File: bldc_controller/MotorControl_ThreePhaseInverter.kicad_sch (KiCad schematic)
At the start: 42 parts, among them J11 Phase A, J12 Phase B, J13 Phase C, Q1 TPH2R408QM,L1Q, Q2 TPH2R408QM,L1Q, Q3 TPH2R408QM,L1Q, Q4 TPH2R408QM,L1Q, Q5 TPH2R408QM,L1Q, Q6 TPH2R408QM,L1Q

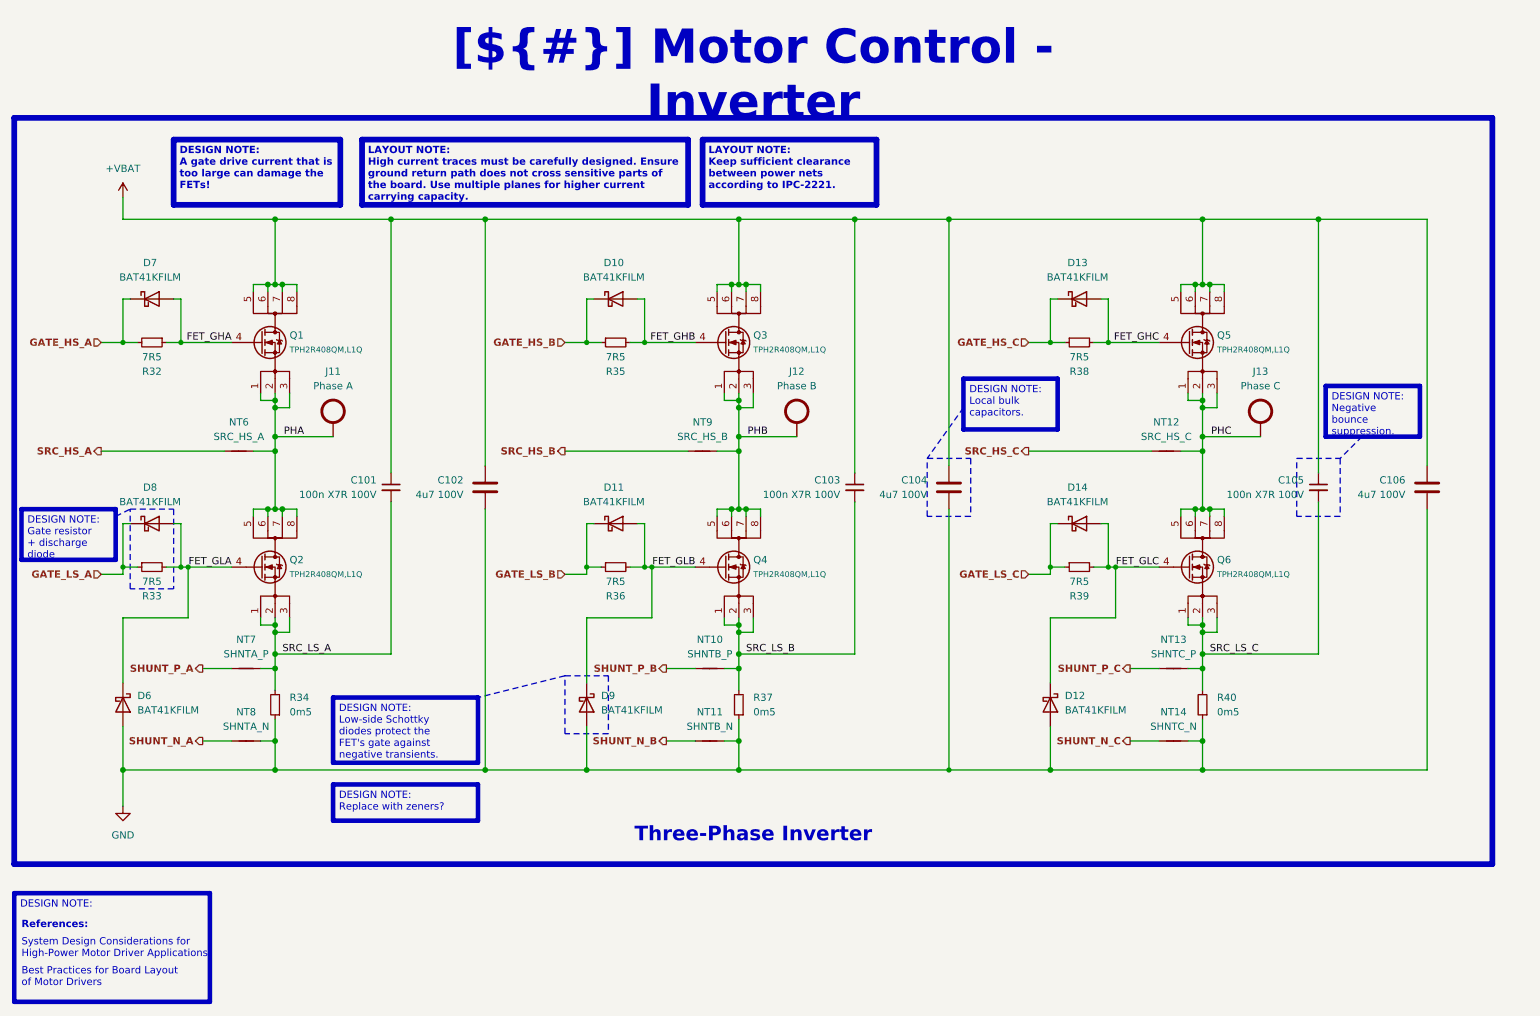
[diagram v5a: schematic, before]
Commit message: routed all signals. TODO: redo all power polygons and ensure good return paths/reference. Added 3d models
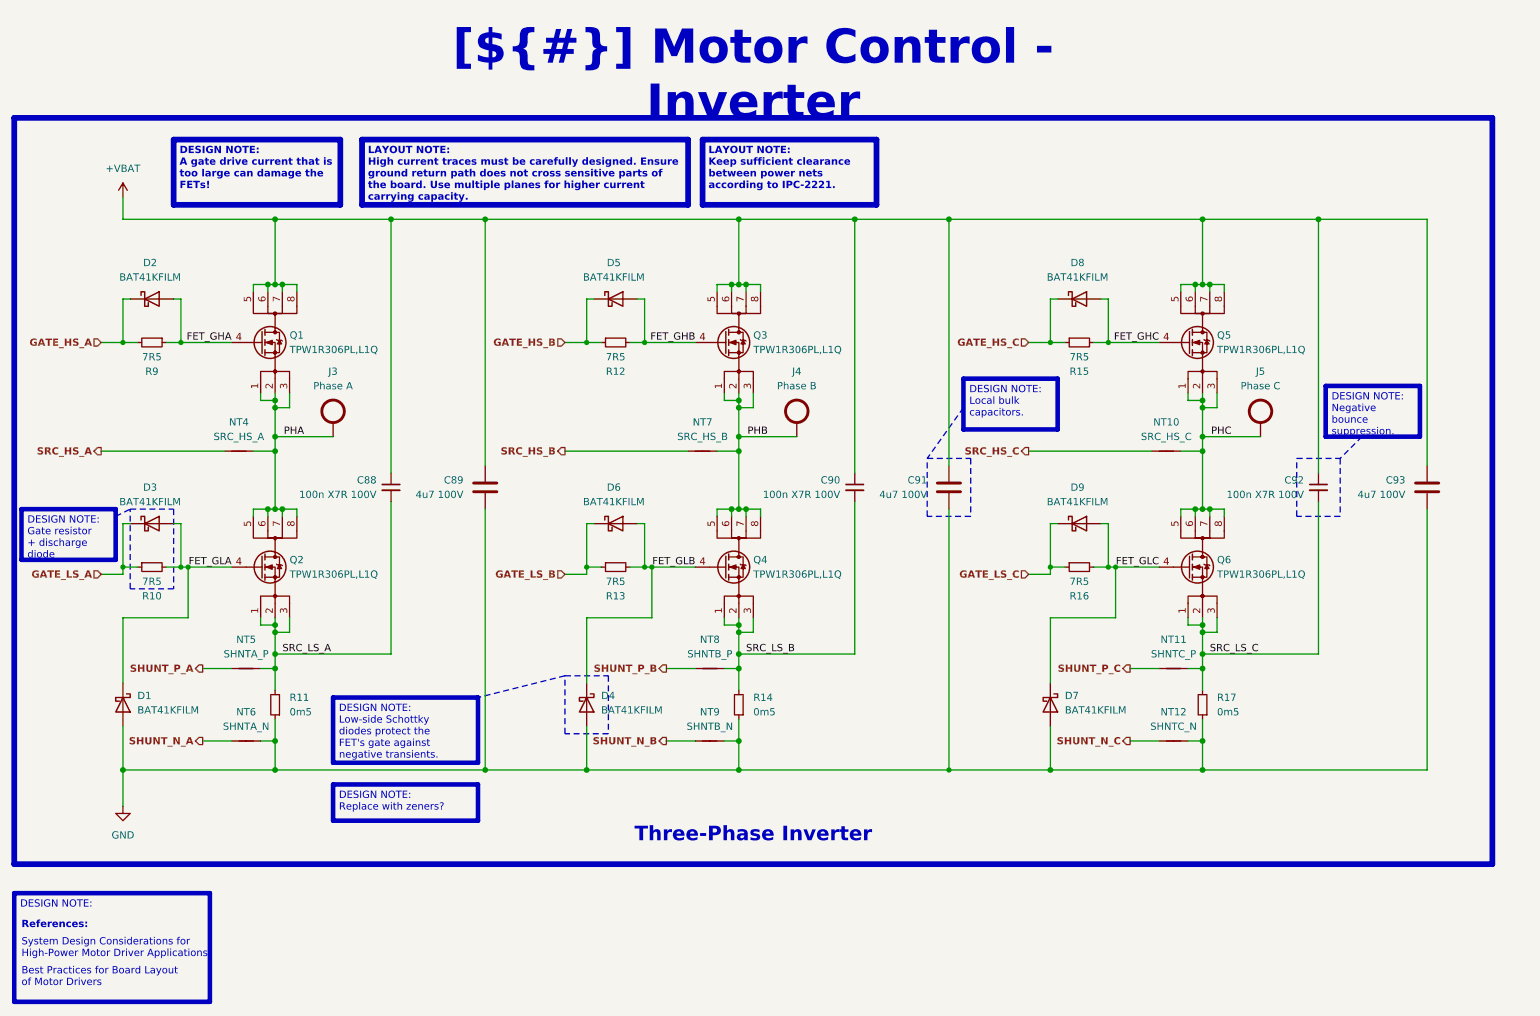
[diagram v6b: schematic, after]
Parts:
- removed Q1, Q2, Q3, Q4, Q5, Q6: TPH2R408QM,L1Q, 0_transistor_fet:2-5Q1S, symbol 0_transistor_fet:TPH2R408QM,L1Q
- added Q1, Q2, Q3, Q4, Q5, Q6: TPW1R306PL,L1Q, 0_transistor_fet:2-5S1A, symbol 0_transistor_fet:TPW1R306PL,L1Q
- renumbered C101 to C88, C102 to C89, C103 to C90, C104 to C91, C105 to C92, C106 to C93, D6 to D1, D7 to D2, D8 to D3, D9 to D4, D10 to D5, D11 to D6, D12 to D7, D13 to D8, D14 to D9, J11 to J3, J12 to J4, J13 to J5, NT12 to NT10, NT13 to NT11, NT14 to NT12, NT6 to NT4, NT7 to NT5, NT8 to NT6, NT9 to NT7, NT10 to NT8, NT11 to NT9, R33 to R10, R34 to R11, R35 to R12, R36 to R13, R37 to R14, R38 to R15, R39 to R16, R40 to R17, R32 to R9
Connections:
- net +VBAT: now also Q1.5 (D), Q1.6 (D), Q1.7 (D), Q1.8 (D), Q3.5 (D), Q3.6 (D), Q3.7 (D), Q3.8 (D), Q5.5 (D), Q5.6 (D), Q5.7 (D), Q5.8 (D)
- net FET_GHA: now also Q1.4 (G)
- net FET_GHB: now also Q3.4 (G)
- net FET_GHC: now also Q5.4 (G)
- net FET_GLA: now also Q2.4 (G)
- net FET_GLB: now also Q4.4 (G)
- net FET_GLC: now also Q6.4 (G)
- net PHA: now also Q1.1 (S), Q1.2 (S), Q1.3 (S), Q2.5 (D), Q2.6 (D), Q2.7 (D), Q2.8 (D)
- net PHB: now also Q3.1 (S), Q3.2 (S), Q3.3 (S), Q4.5 (D), Q4.6 (D), Q4.7 (D), Q4.8 (D)
- net PHC: now also Q5.1 (S), Q5.2 (S), Q5.3 (S), Q6.5 (D), Q6.6 (D), Q6.7 (D), Q6.8 (D)
- net SRC_LS_A: now also Q2.1 (S), Q2.2 (S), Q2.3 (S)
- net SRC_LS_B: now also Q4.1 (S), Q4.2 (S), Q4.3 (S)
- net SRC_LS_C: now also Q6.1 (S), Q6.2 (S), Q6.3 (S)

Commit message: started routing polygons
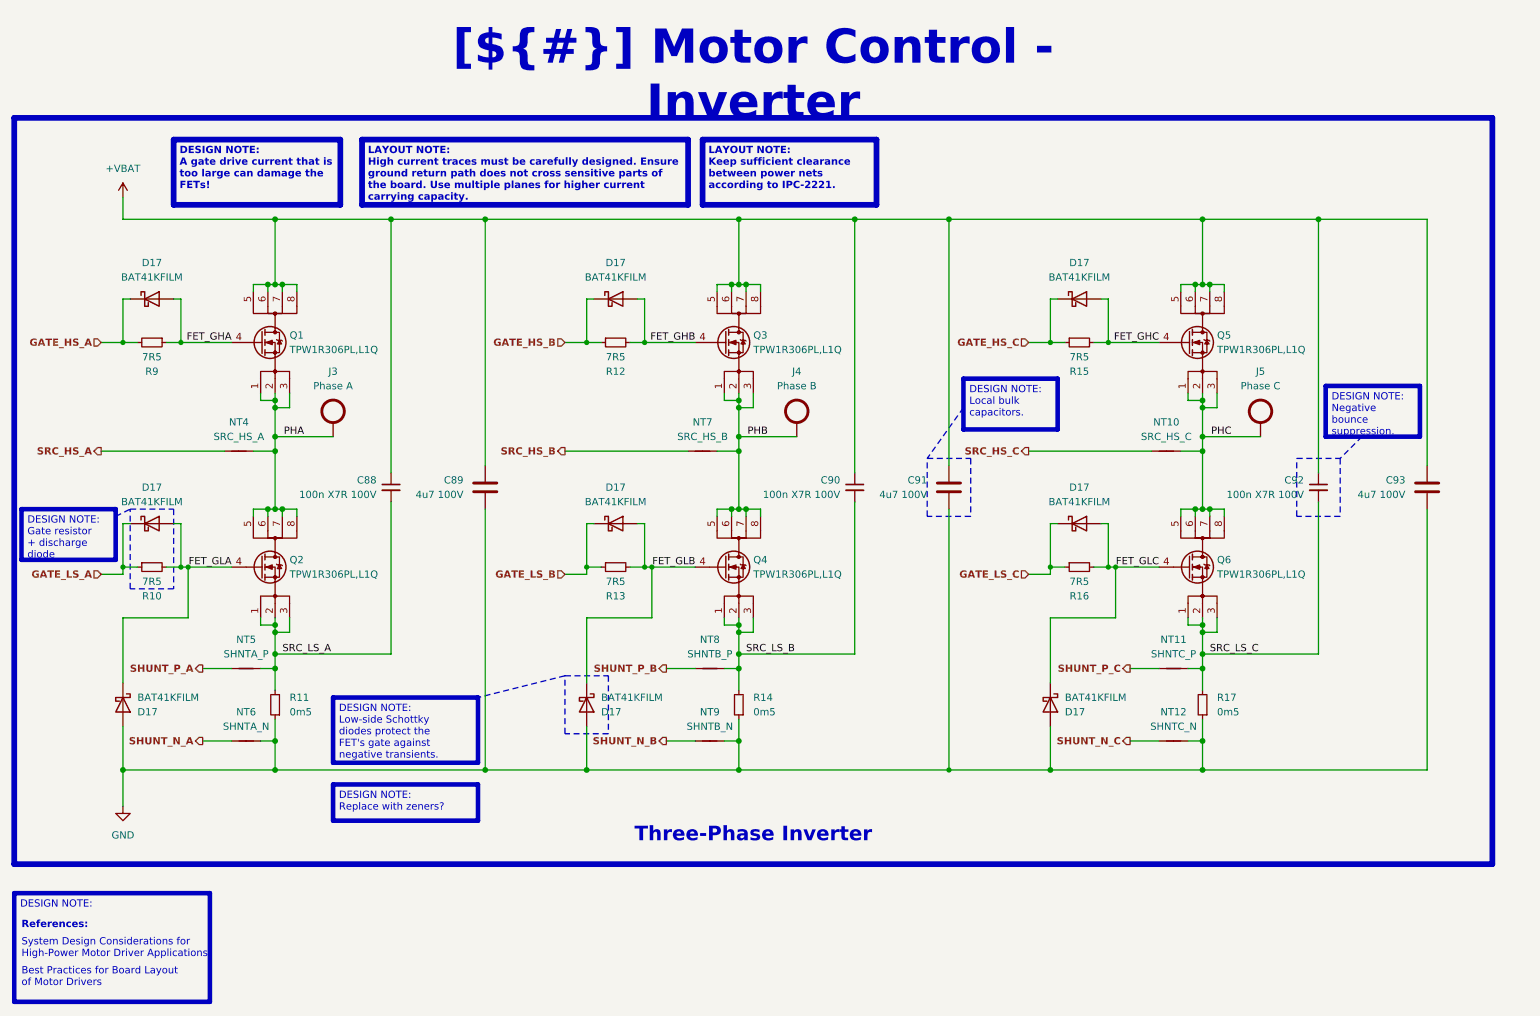
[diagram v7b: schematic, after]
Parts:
- removed D1, D2, D3, D4, D5, D6, D7, D8, D9: BAT41KFILM, Diode_SMD:D_SOD-523, symbol 0_diode:BAT41KFILM
- added D17 (x9): BAT41KFILM, 0_diode_smd:D_SOD-523, symbol 0_diode:BAT41KFILM
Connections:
- net FET_GHA: now also D17.2 (A)
- net FET_GHB: now also D17.2 (A)
- net FET_GHC: now also D17.2 (A)
- net FET_GLA: now also D17.1 (K), D17.2 (A)
- net FET_GLB: now also D17.1 (K), D17.2 (A)
- net FET_GLC: now also D17.1 (K), D17.2 (A)
- net GATE_HS_A: now also D17.1 (K)
- net GATE_HS_B: now also D17.1 (K)
- net GATE_HS_C: now also D17.1 (K)
- net GATE_LS_A: now also D17.1 (K)
- net GATE_LS_B: now also D17.1 (K)
- net GATE_LS_C: now also D17.1 (K)
- net GND: now also D17.2 (A), D17.2 (A), D17.2 (A)

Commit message: Added block diagram, currently rerouting power polygons
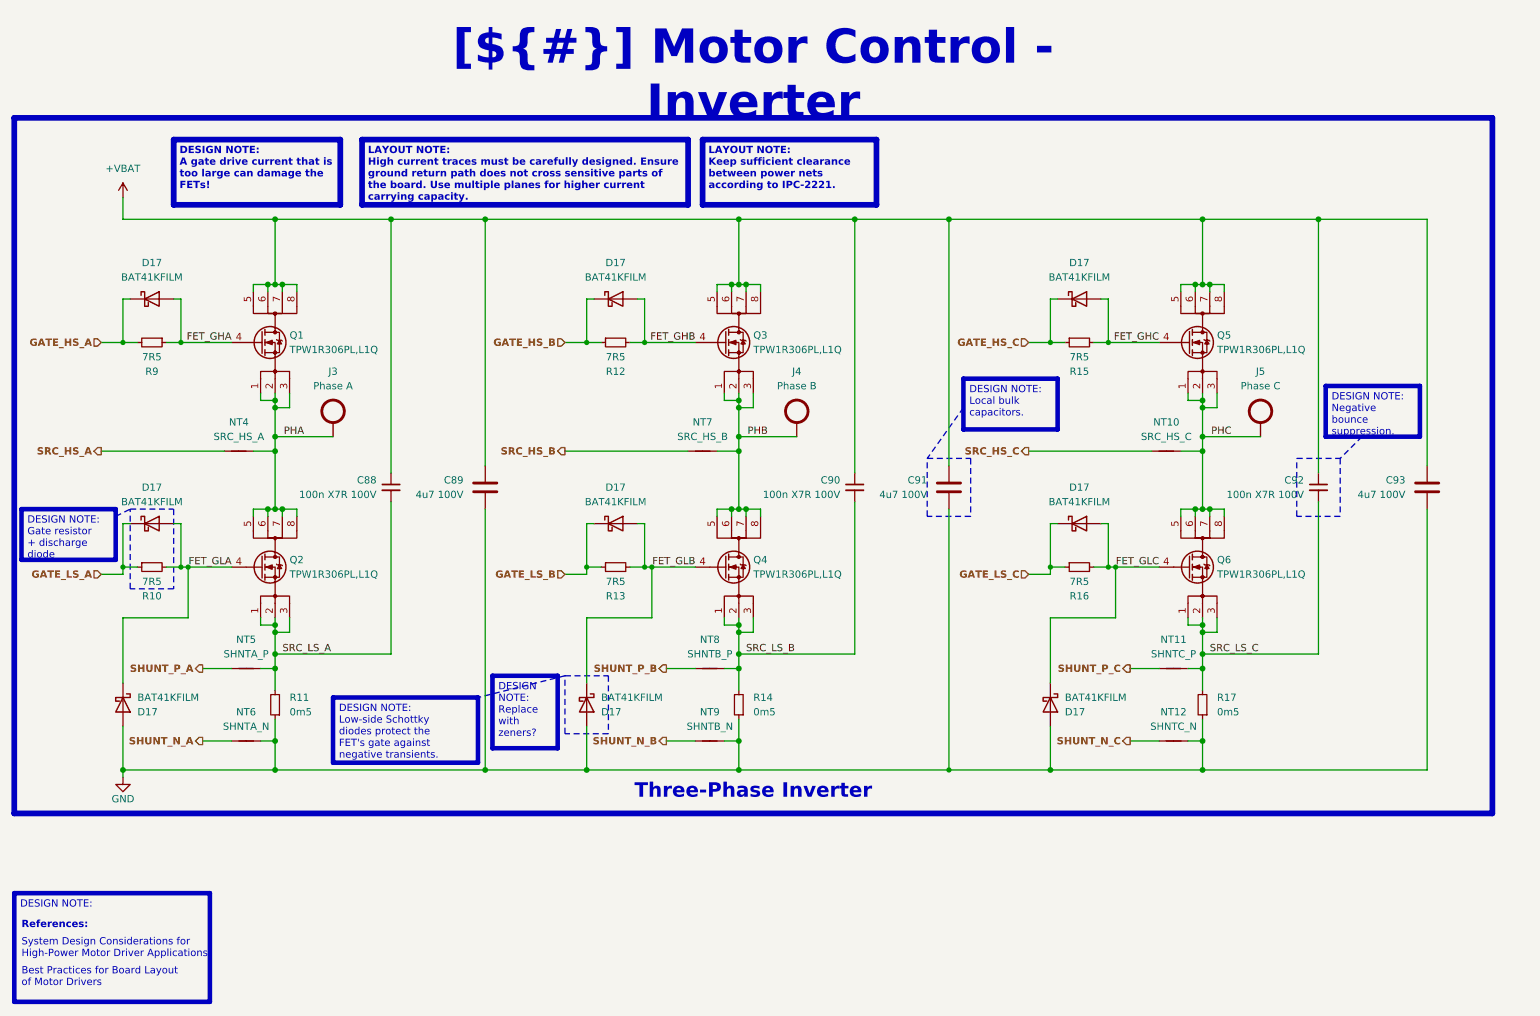
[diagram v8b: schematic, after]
